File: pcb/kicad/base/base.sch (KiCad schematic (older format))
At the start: 52 parts, among them P1 J-Link SWD, P10 CONN_01X02, P11 CONN_01X02, P2 SMA, P3 CONN_01X02, P4 USB Micro B, Q1 IRLML2502, U1 SAMB11G18A-edit, U2 XBee-PRO_900HP, Y1 32.768kHz, Y2 26MHz

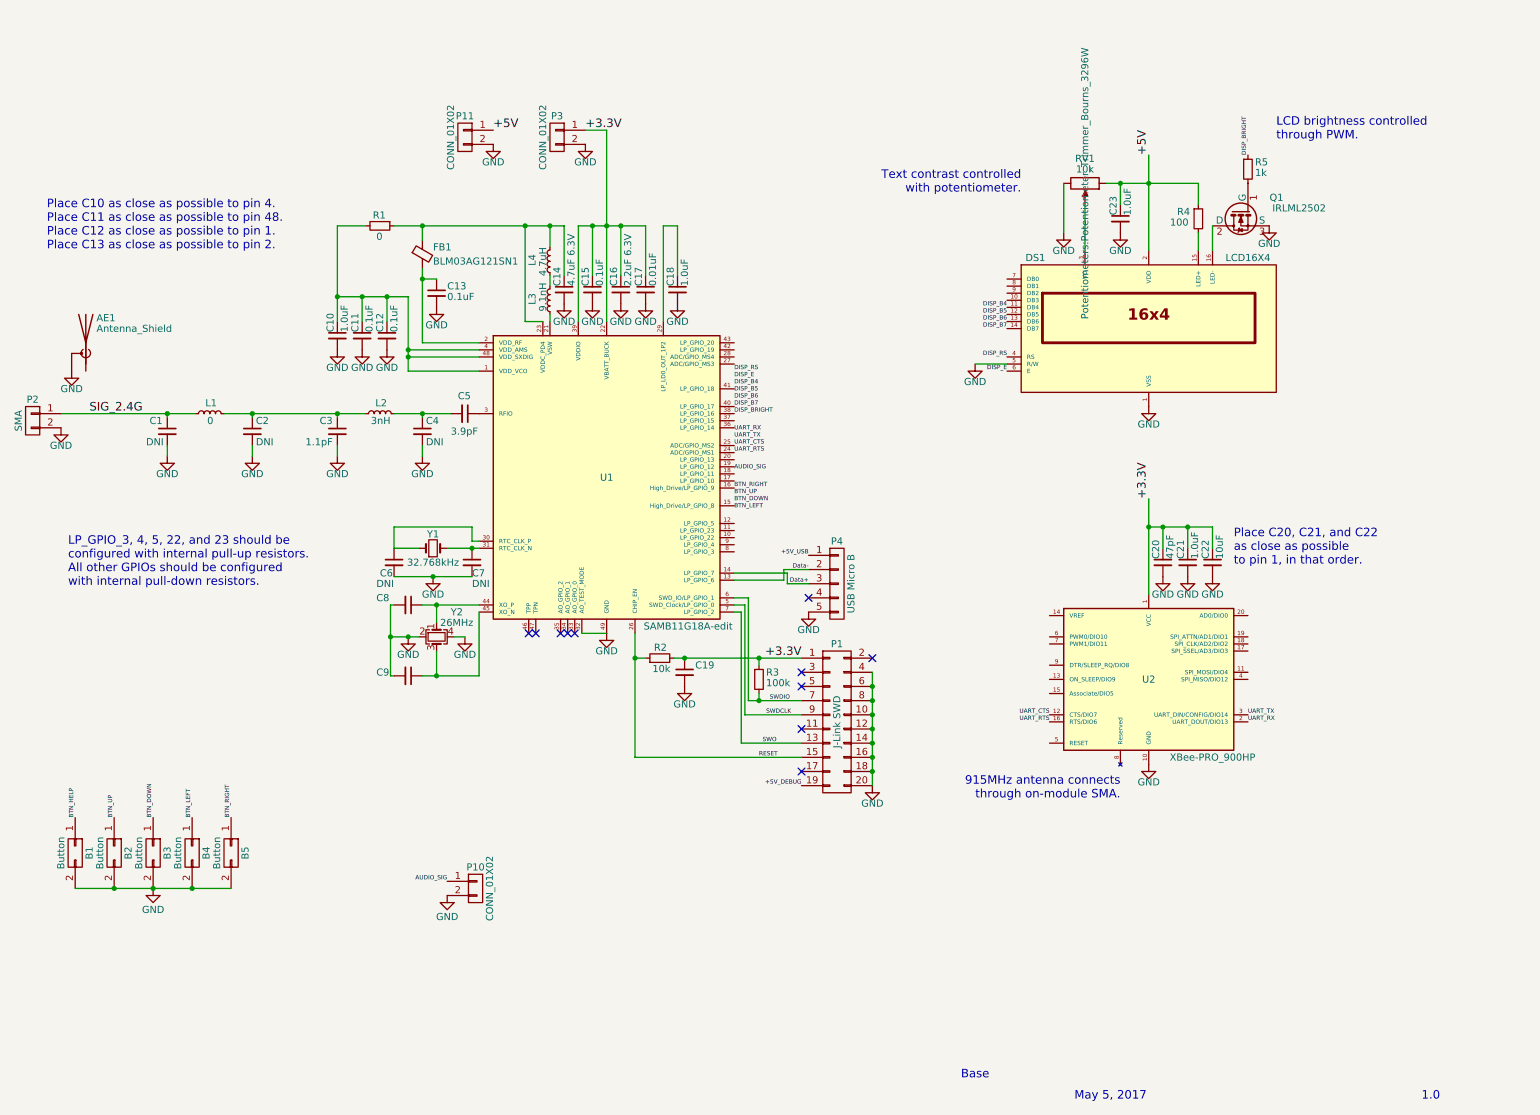
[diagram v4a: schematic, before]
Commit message: Add stitch vias and fix silkscreen identifiers
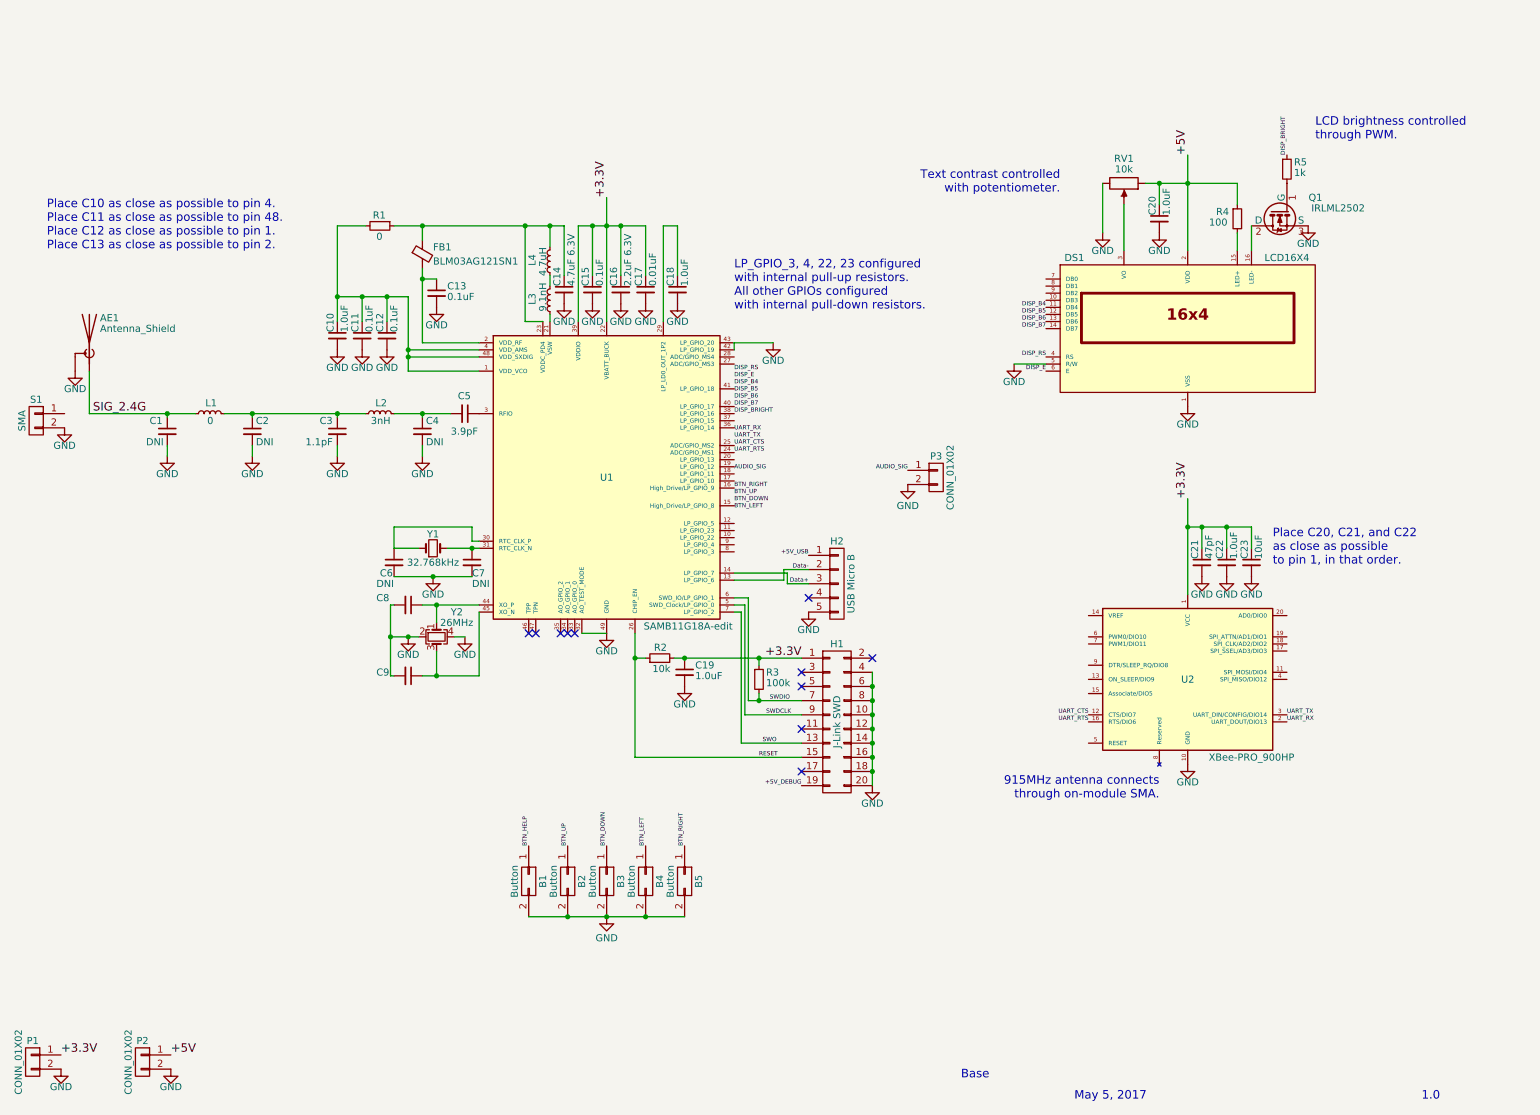
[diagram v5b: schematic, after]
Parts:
- C19: value C_Small -> 1.0uF
- DS1: footprint CFAH1604A -> Displays:CFAH1604A
- U2: footprint Digi_XBee-PRO_TH -> RF_Modules:Digi_XBee-PRO_TH
- renumbered C23 to C20, C20 to C21, C21 to C22, C22 to C23, P1 to H1, P4 to H2, P3 to P1, P11 to P2, P10 to P3, P2 to S1
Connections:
- net GND: now also U1.42 (LP_GPIO_19), U1.43 (LP_GPIO_20)
- net SIG_2.4G: now also AE1.1 (A); no longer S1.1 (P1)
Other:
- note added: "LP_GPIO_3, 4, 22, 23 configured\nwith internal pull-up resistors.\nAll other GPIOs configured\nwith internal pull-down resistors."
- note removed: "LP_GPIO_3, 4, 5, 22, and 23 should be\nconfigured with internal pull-up resistors.\nAll other GPIOs should be configured\nwith internal pull-down resistors."
- moved on the sheet: AE1, B1, B2, B3, B4, B5, C20, C21, C22, C23, DS1, P1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

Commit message: Add vertical SMA, matching stub, and dimensions
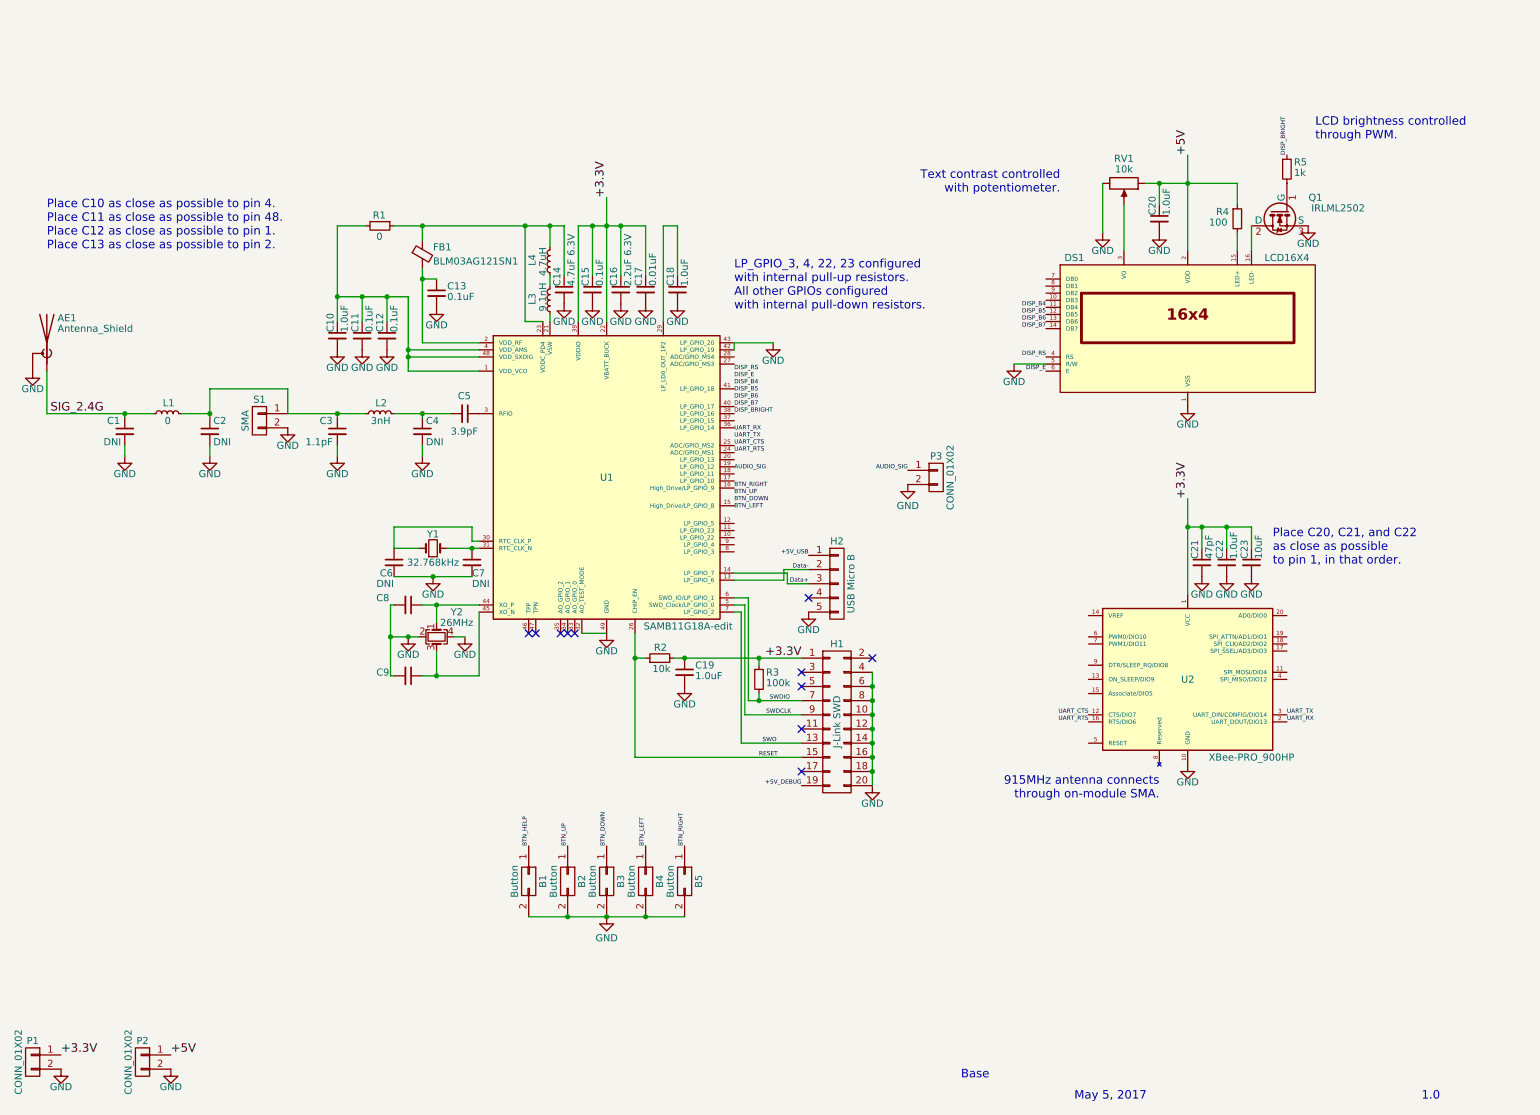
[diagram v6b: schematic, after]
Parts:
- S1: footprint Misc:Molex_SMA_Jack_Edge_Mount -> Misc:Linx_SMA_Jack_Vert_Mount
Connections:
- net at C2.1, C3.1, L1.2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: now also S1.1 (P1)
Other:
- moved on the sheet: AE1, C1, C2, L1, S1

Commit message: Fix footprints for connectors and crystal
Unnecessary SMDs in the matching circuit and 0 ohm link removed from the
schematic. Certain resistor and capacitor values updated to new offical
BOM components.
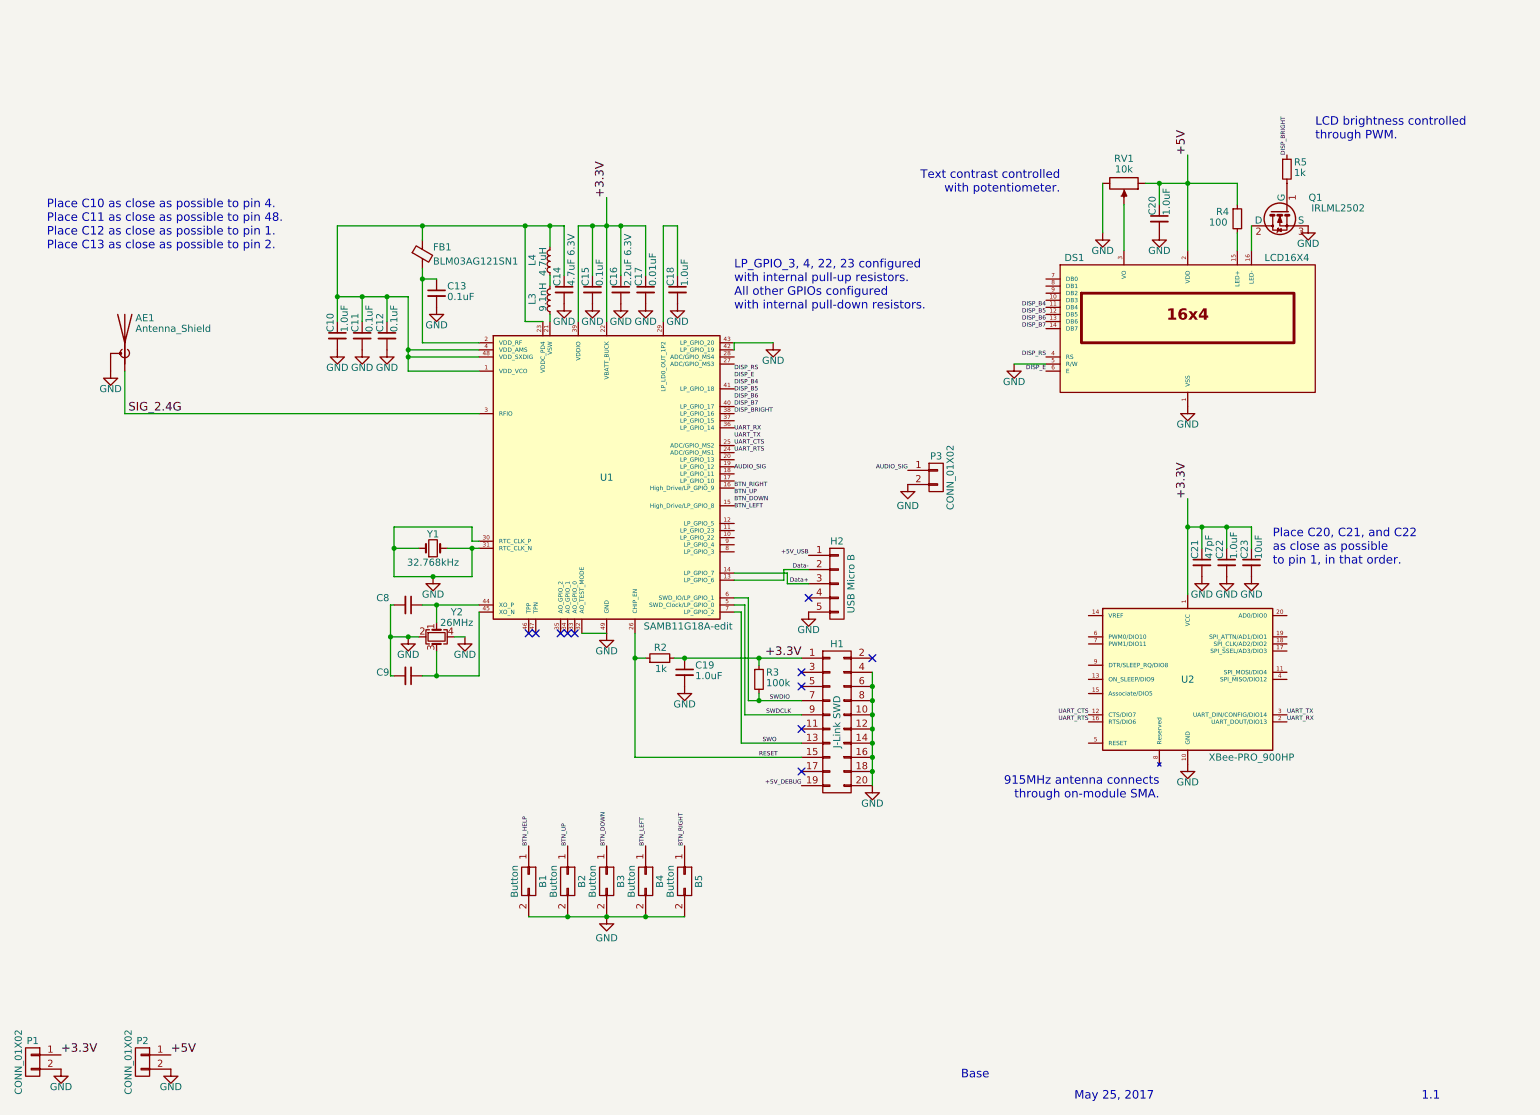
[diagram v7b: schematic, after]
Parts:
- removed C1, C2, C4, C6, C7: DNI, Capacitors_SMD:C_0402, symbol C_Small
- removed C3: 1.1pF, Capacitors_SMD:C_0402, symbol C_Small
- removed C5: 3.9pF, Capacitors_SMD:C_0402, symbol C_Small
- removed L1: 0, Capacitors_SMD:C_0402, symbol L_Small
- removed L2: 3nH, Capacitors_SMD:C_0402, symbol L_Small
- removed R1: 0, Capacitors_SMD:C_0402, symbol R_Small
- removed S1: SMA, Misc:Linx_SMA_Jack_Vert_Mount, symbol CONN_01X02
- H1: footprint Misc:Socket_Strip_Straight_2x10_Pitch2.54mm_Drill0.762mm -> Misc:Socket_Strip_Straight_2x10_Pitch2.54mm_Drill0.889mm
- P1, P2, P3: footprint Misc:Socket_Strip_Straight_1x02_Pitch2.54mm_Drill0.762mm -> Connectors:OSTTEXX0164_2pin_3.5mm
- R2: value 10k -> 1k
- Y2: footprint Crystals:Crystal_SMD_2520-4pin_2.5x2.0mm -> Crystals:Crystal_SMD_3225-4pin_3.2x2.5mm
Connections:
- net GND: now also U1.30 (RTC_CLK_P), U1.31 (RTC_CLK_N), Y1.1, Y1.2
- net SIG_2.4G: now also U1.3 (RFIO)
- net at C14.1, FB1.1, L4.2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: now also C10.1, C11.1, C12.1, U1.1 (VDD_VCO), U1.4 (VDD_AMS), U1.48 (VDD_SXDIG)
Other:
- note added: "1.1"
- note added: "May 25, 2017"
- note removed: "1.0"
- note removed: "May 5, 2017"
- moved on the sheet: AE1

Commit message: Move several components and traces around
All components except SWD have been connected. May want to route SWD and
button signals on opposite sides.
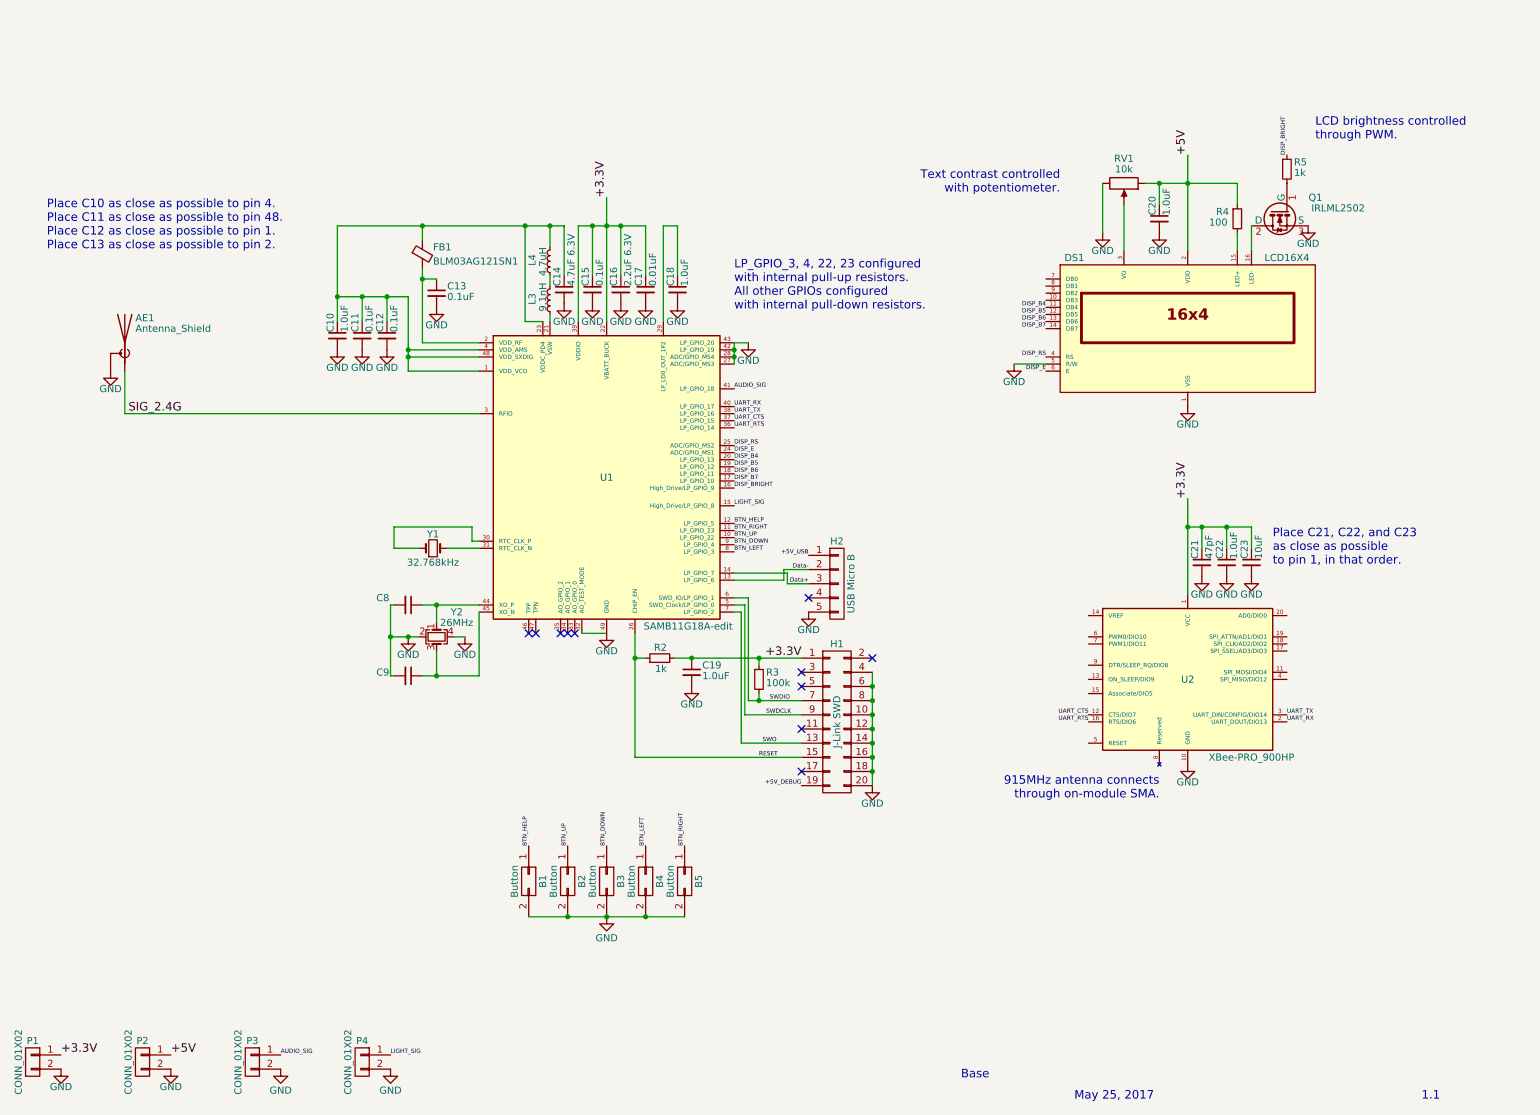
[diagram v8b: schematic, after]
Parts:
- added P4: CONN_01X02, Connectors:OSTTEXX0164_2pin_3.5mm, symbol CONN_01X02
- RV1: footprint Potentiometers:Potentiometer_Trimmer_Bourns_3296W -> Misc:Potentiometer_Trimmer_Bourns_3309W
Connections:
- net AUDIO_SIG: now also U1.41 (LP_GPIO_18)
- net BTN_DOWN: now also U1.9 (LP_GPIO_4)
- net BTN_HELP: now also U1.12 (LP_GPIO_5)
- net BTN_LEFT: now also U1.8 (LP_GPIO_3)
- net BTN_RIGHT: now also U1.11 (LP_GPIO_23); no longer U1.16 (High_Drive/LP_GPIO_9)
- net BTN_UP: now also U1.10 (LP_GPIO_22)
- net DISP_B4: now also U1.20 (LP_GPIO_13)
- net DISP_B5: now also U1.19 (LP_GPIO_12)
- net DISP_B6: now also U1.18 (LP_GPIO_11)
- net DISP_B7: now also U1.17 (LP_GPIO_10); no longer U1.40 (LP_GPIO_17)
- net DISP_BRIGHT: now also U1.16 (High_Drive/LP_GPIO_9); no longer U1.38 (LP_GPIO_16)
- net DISP_E: now also U1.24 (ADC/GPIO_MS1)
- net DISP_RS: now also U1.25 (ADC/GPIO_MS2)
- net GND: now also U1.27 (ADC/GPIO_MS3), U1.28 (ADC/GPIO_MS4), P4.2 (P2); no longer U1.30 (RTC_CLK_P), U1.31 (RTC_CLK_N), Y1.1, Y1.2
- net UART_CTS: now also U1.37 (LP_GPIO_15); no longer U1.25 (ADC/GPIO_MS2)
- net UART_RTS: now also U1.36 (LP_GPIO_14); no longer U1.24 (ADC/GPIO_MS1)
- net UART_RX: now also U1.40 (LP_GPIO_17)
- net UART_TX: now also U1.38 (LP_GPIO_16)
- net LIGHT_SIG: now reaches U1.15 (High_Drive/LP_GPIO_8)
- net LIGHT_SIG: now also P4.1 (P1)
- new net: U1.30 (RTC_CLK_P), Y1.1
- new net: U1.31 (RTC_CLK_N), Y1.2
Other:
- note added: "Place C21, C22, and C23\nas close as possible\nto pin 1, in that order."
- note removed: "Place C20, C21, and C22\nas close as possible\nto pin 1, in that order."
- moved on the sheet: C19, P3
